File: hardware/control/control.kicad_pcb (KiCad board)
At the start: 2 copper layers, 110 x 70 mm, 58 parts, among them J1 Conn_01x05_Male, J2 CANPWR, J3 CANGND, J4 RJ45, J5 RJ45, J6 Conn_02x03_Odd_Even, J7 DCDC-PWM, J8 DCDC-MEASURES, J9 display, Q1 BSS123, SW1 next, SW2 select, U1 2.048V, U2 AP63200WU, U3 PIC18F27Q84, U4 TLE9250VSJXUMA1, Y1 10Mhz

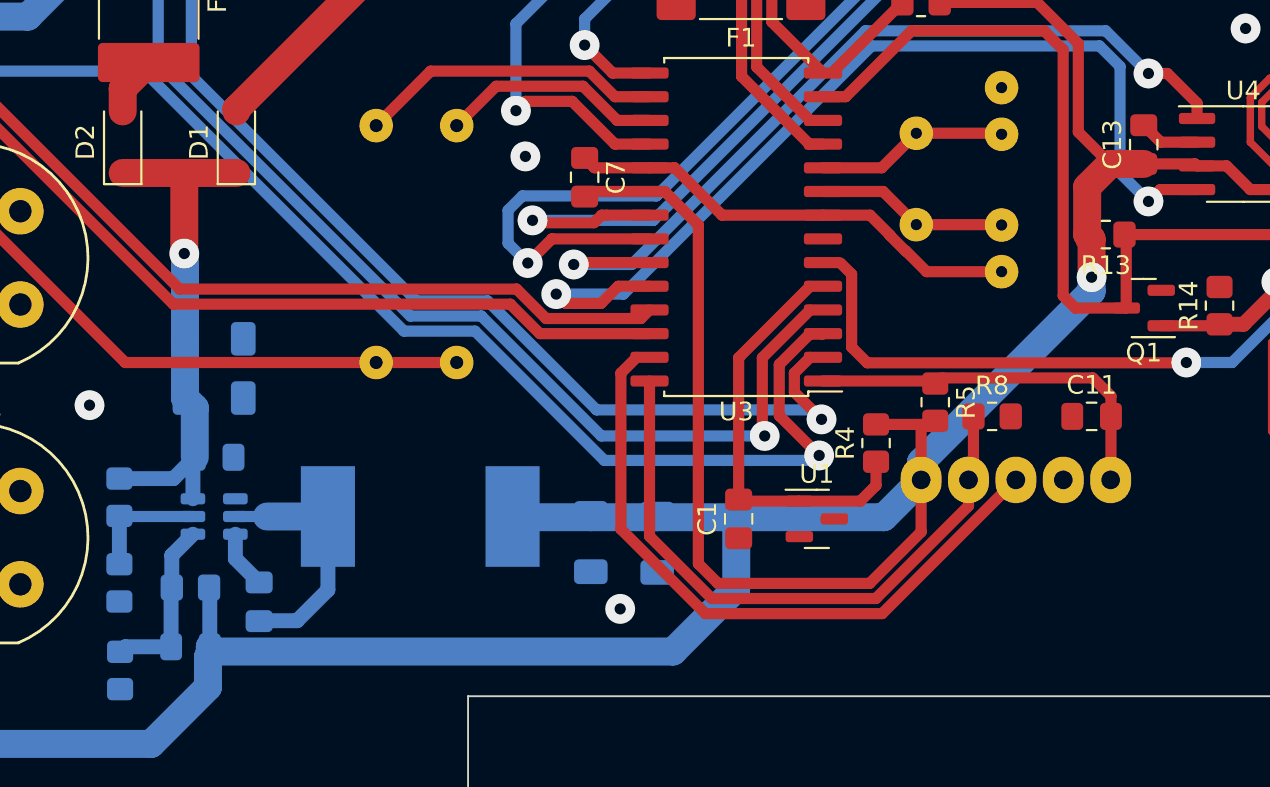
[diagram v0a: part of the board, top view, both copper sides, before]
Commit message: Adjust PCBs after reference and footprint changes
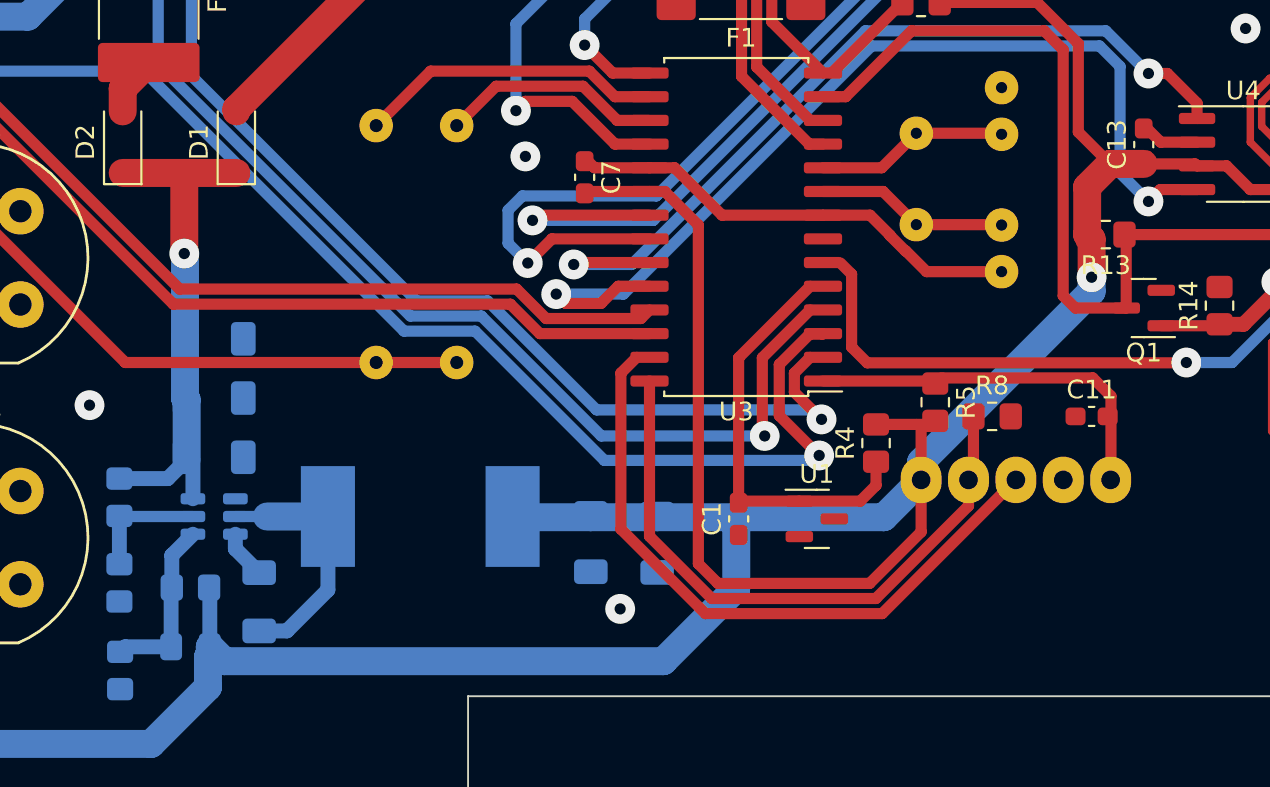
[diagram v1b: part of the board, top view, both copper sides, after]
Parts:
- C1, C11, C13, C7: footprint Capacitor_SMD:C_0805_2012Metric_Pad1.18x1.45mm_HandSolder -> Capacitor_SMD:C_0603_1608Metric_Pad1.08x0.95mm_HandSolder
- C4, C8: footprint Capacitor_SMD:C_0805_2012Metric_Pad1.18x1.45mm_HandSolder -> Capacitor_SMD:C_1206_3216Metric_Pad1.33x1.80mm_HandSolder
- R17: value 22k -> 22k
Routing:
- net Net-(C2-Pad1): track 28.3 -> 27.7 mm
- net Net-(C8-Pad2): track 3.11 -> 2.59 mm

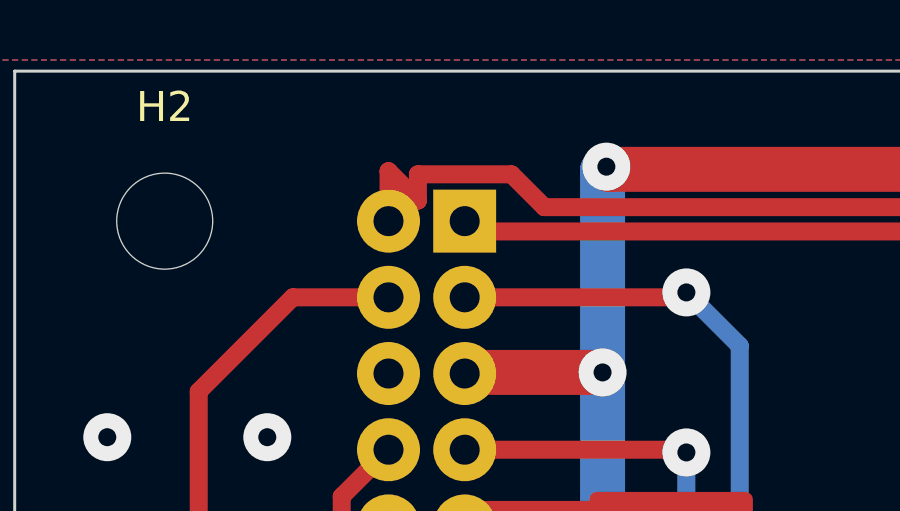
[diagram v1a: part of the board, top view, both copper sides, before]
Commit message: Adjust track near connector
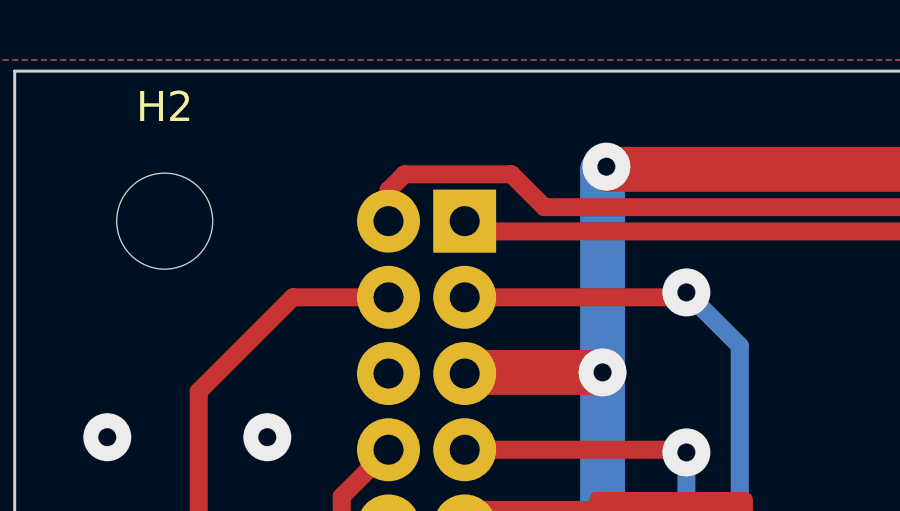
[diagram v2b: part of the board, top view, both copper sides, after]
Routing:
- net /PWM_OFF: track 62.1 -> 60.4 mm
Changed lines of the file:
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@@
   (segment (start 103.663 102.774) (end 103.663 93.632512) (width 0.6) (layer "F.Cu") (net 38))
   (segment (start 107.2905 106.4015) (end 103.663 102.774) (width 0.6) (layer "F.Cu") (net 38))
-  (segment (start 62.46 83.336) (end 62.46 85) (width 0.6) (layer "F.Cu") (net 39))
-  (segment (start 66.56 83.44) (end 63.44 83.44) (width 0.6) (layer "F.Cu") (net 39))
-  (segment (start 63.44 84.316) (end 62.46 83.336) (width 0.6) (layer "F.Cu") (net 39))
+  (segment (start 62.991 83.44) (end 62.46 83.971) (width 0.6) (layer "F.Cu") (net 39))
+  (segment (start 107.339619 105.1315) (end 104.473 102.264881) (width 0.6) (layer "F.Cu") (net 39))
+  (segment (start 62.46 83.971) (end 62.46 85) (width 0.6) (layer "F.Cu") (net 39))
+  (segment (start 67.654 84.534) (end 66.56 83.44) (width 0.6) (layer "F.Cu") (net 39))
+  (segment (start 95.71 84.534) (end 67.654 84.534) (width 0.6) (layer "F.Cu") (net 39))
+  (segment (start 104.473 93.297) (end 95.71 84.534) (width 0.6) (layer "F.Cu") (net 39))
+  (segment (start 66.56 83.44) (end 62.991 83.44) (width 0.6) (layer "F.Cu") (net 39))
   (segment (start 104.473 102.264881) (end 104.473 93.297) (width 0.6) (layer "F.Cu") (net 39))
-  (segment (start 95.71 84.534) (end 67.654 84.534) (width 0.6) (layer "F.Cu") (net 39))
-  (segment (start 107.339619 105.1315) (end 104.473 102.264881) (width 0.6) (layer "F.Cu") (net 39))
-  (segment (start 63.44 83.44) (end 63.44 84.316) (width 0.6) (layer "F.Cu") (net 39))
-  (segment (start 104.473 93.297) (end 95.71 84.534) (width 0.6) (layer "F.Cu") (net 39))
-  (segment (start 67.654 84.534) (end 66.56 83.44) (width 0.6) (layer "F.Cu") (net 39))
   (segment (start 123.093 92.067) (end 127.62 87.54) (width 0.6) (layer "F.Cu") (net 40))
   (segment (start 105.156 91.948) (end 105.275 92.067) (width 0.6) (layer "F.Cu") (net 40))

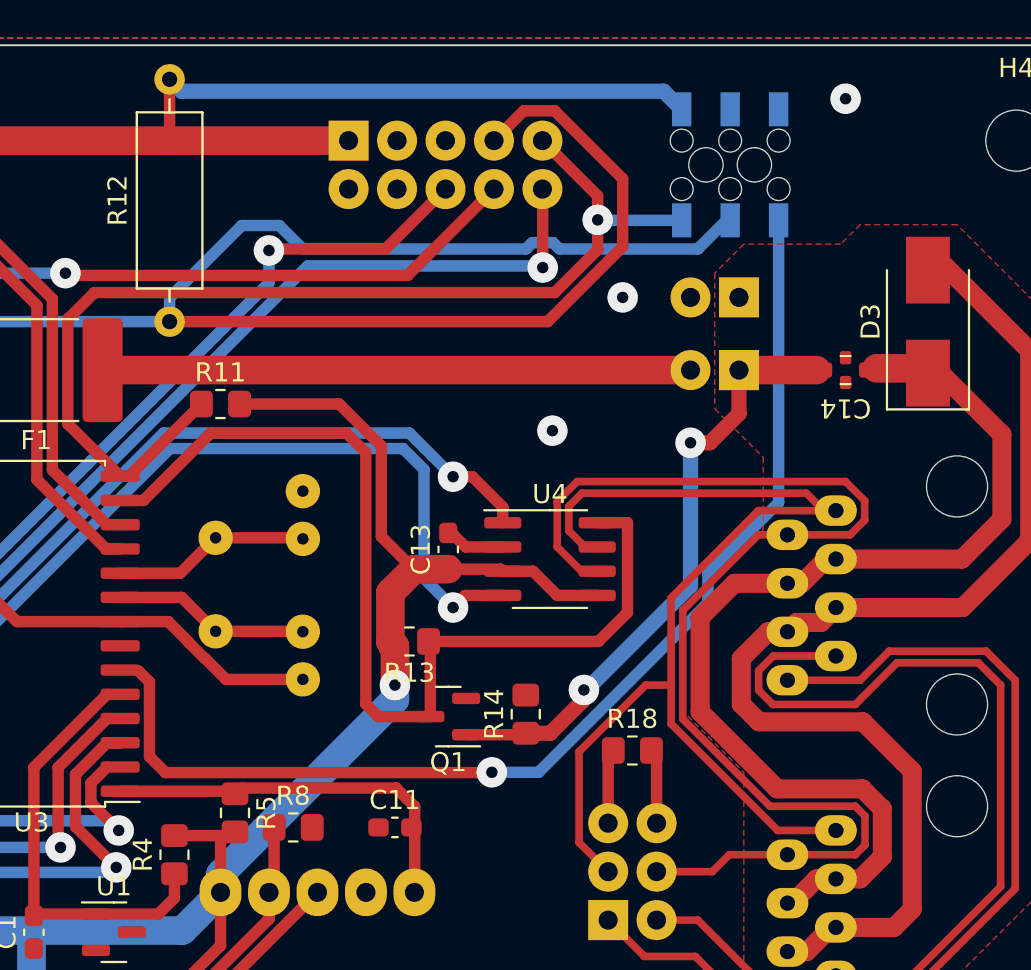
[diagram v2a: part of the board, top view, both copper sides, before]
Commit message: Route unused RA5 to display and power board connectors, "just in case"
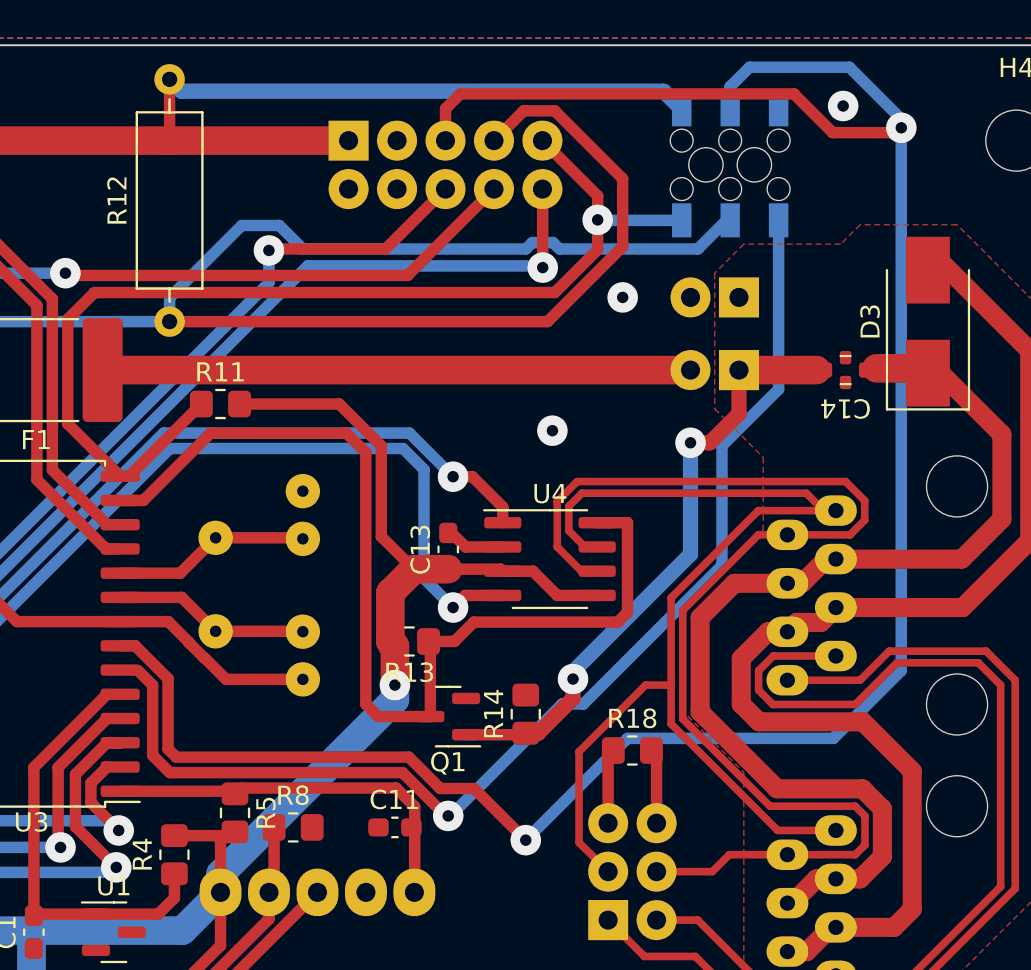
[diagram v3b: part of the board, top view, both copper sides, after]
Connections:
- J8 pad 5: unconnected-(J8-Pad5) -> RA5
- J9 pad 2: unconnected-(J9-Pad2) -> RA5
- U3 pad 7: GND -> RA5
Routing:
- net RA5: track 0.00 -> 118.4 mm, vias 0 -> 2
- net ~{RST_DISP}: track 59.7 -> 60.7 mm
